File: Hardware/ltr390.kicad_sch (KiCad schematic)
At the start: 3 parts, among them U3 LTR-390UV

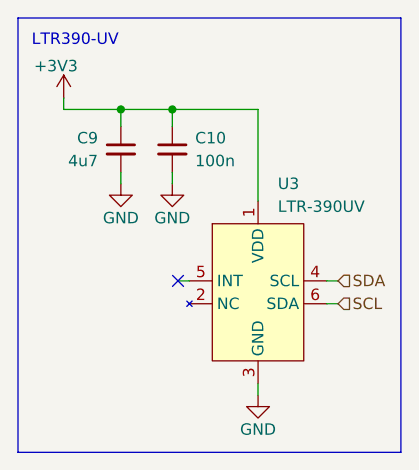
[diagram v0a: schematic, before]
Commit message: Swapped SCL und SDA for LTR (fucked up)
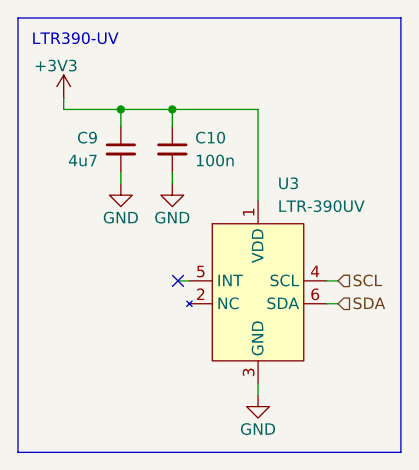
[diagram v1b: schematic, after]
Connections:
- net SCL: now also U3.4 (SCL); no longer U3.6 (SDA)
- net SDA: now also U3.6 (SDA); no longer U3.4 (SCL)
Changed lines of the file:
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@@
 	(hierarchical_label "SCL"
 		(shape input)
-		(at 154.305 111.125 0)
+		(at 154.305 108.585 0)
 		(effects
 			(font
@@
 	(hierarchical_label "SDA"
 		(shape input)
-		(at 154.305 108.585 0)
+		(at 154.305 111.125 0)
 		(effects
 			(font
